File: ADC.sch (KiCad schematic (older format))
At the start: 15 parts

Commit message: Added multiple inputs
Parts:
- added C?: 47n, symbol C
- added C?: 4.7n, symbol C
- added C?: 4,7n, symbol C
- added C? (x7): 1n, symbol C
- added C?: 1u, symbol C
- added D? (x7): TVS, symbol TVS
- added P? (x3): CONN_01X03, symbol CONN_01X03
- added R? (x2): 4,7k, symbol R
- R?: value 1,65k -> 820
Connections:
- net +3V3: no longer U?.22 (AVDD)
- net GND: now also U?.10 (VREFCOM), U?.3 (CLK), C?.2
- net GNDA: now also C?.1, C?.1, C?.1, C?.1, C?.2, C?.2, C?.2, C?.2, D?.1, D?.1, D?.1, D?.1, D?.2, D?.2, D?.2
- net Iexc1: now reaches C?.1, C?.2, U?.11 (AIN0)
- net Iexc1: now also P?.2 (P2), U?.20 (IEXC1), C?.2, D?.2; no longer R?.1
- net at U?.13 (AIN4): now also C?.2, D?.2, P?.2 (P2)
- net at U?.14 (AIN5): now also C?.1, D?.1, P?.1 (P1)
- net at U?.15 (AIN6): now also C?.2, D?.2, P?.2 (P2)
- net at U?.16 (AIN7): now also C?.1, D?.1, P?.1 (P1)
- net at U?.17 (AIN2): now also C?.1, C?.2, R?.1
- net at U?.18 (AIN3): now also C?.1, C?.2, R?.1
- net Iexc2: now reaches U?.19 (IEXC2)
- net Iexc2: now also C?.1, D?.1, P?.1 (P1), R?.2
- net at U?.9 (VREFOUT): now also C?.1
- net at R?.2: no longer P?.2 (P2)
- net Vref: now reaches P?.3 (P3), R?.2, R?.2
- net Vref: now also P?.3 (P3), P?.3 (P3), P?.3 (P3)
- new net: C?.2, D?.2, P?.2 (P2), R?.2
- new net: C?.1, D?.1, P?.1 (P1), R?.2
- new net VDDA: U?.22 (AVDD)
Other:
- moved on the sheet: C?, D?, P?, R?

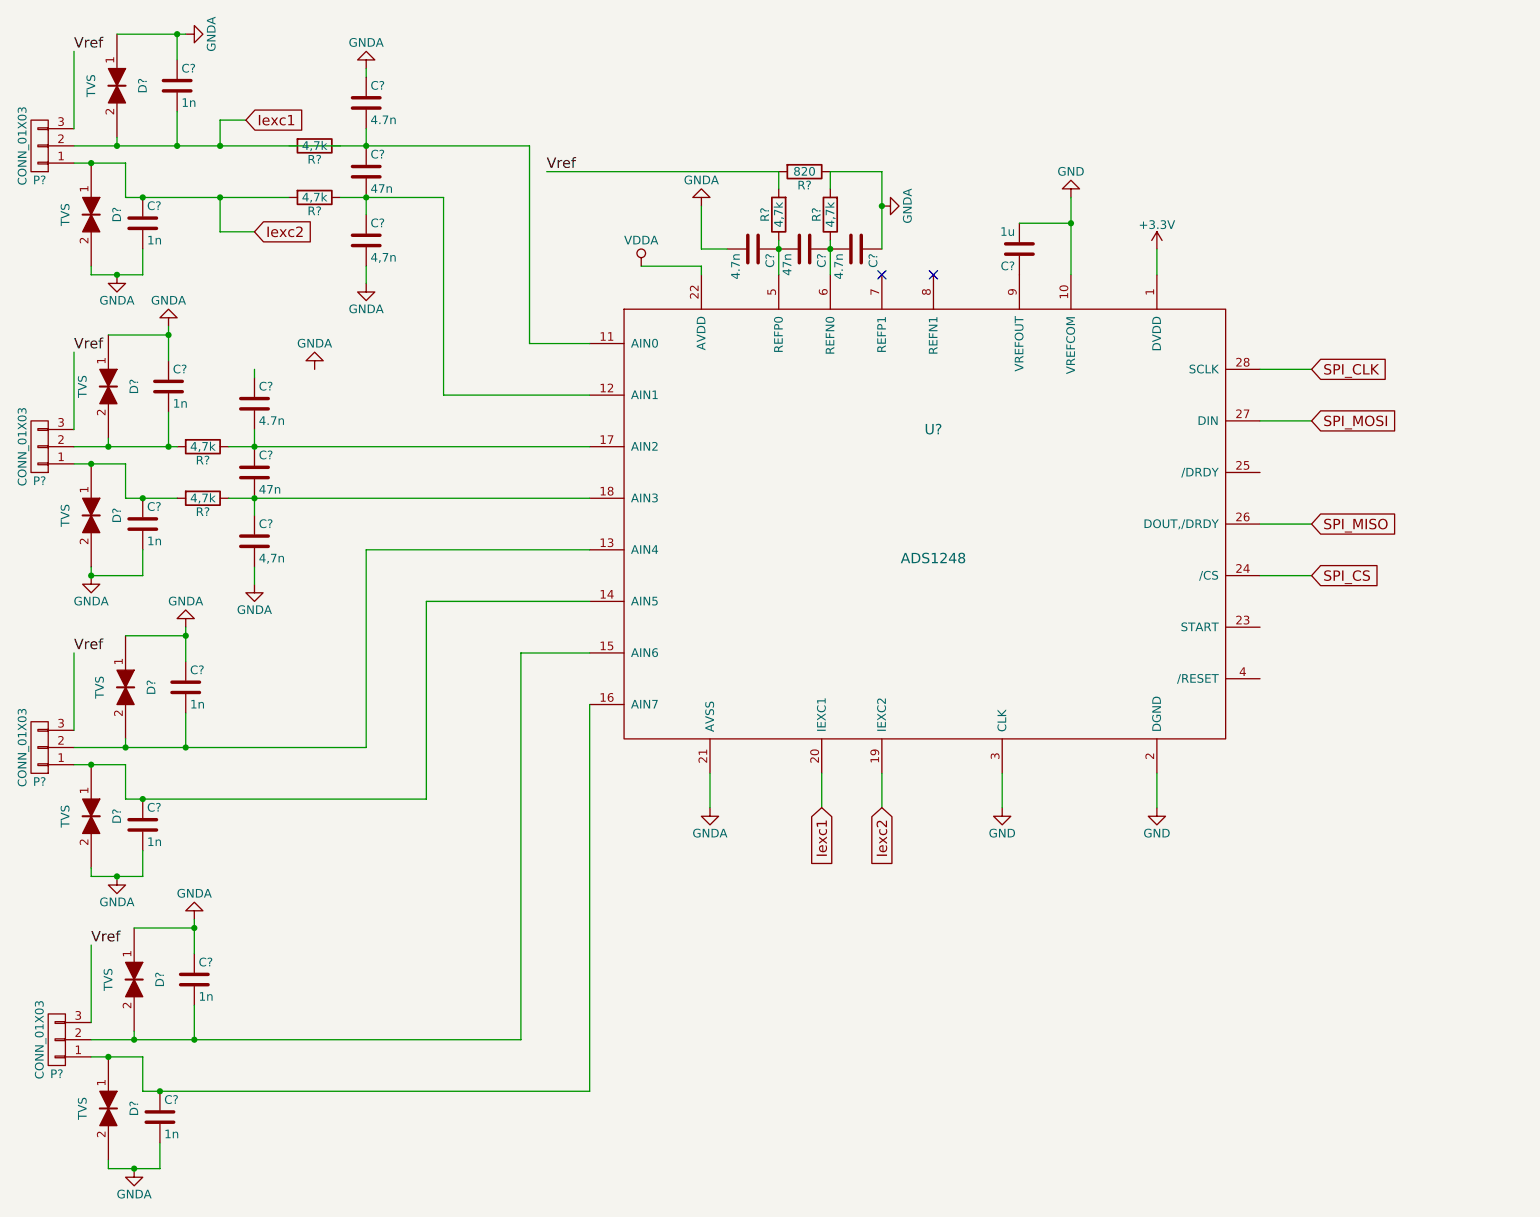
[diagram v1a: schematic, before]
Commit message: Peripherals added
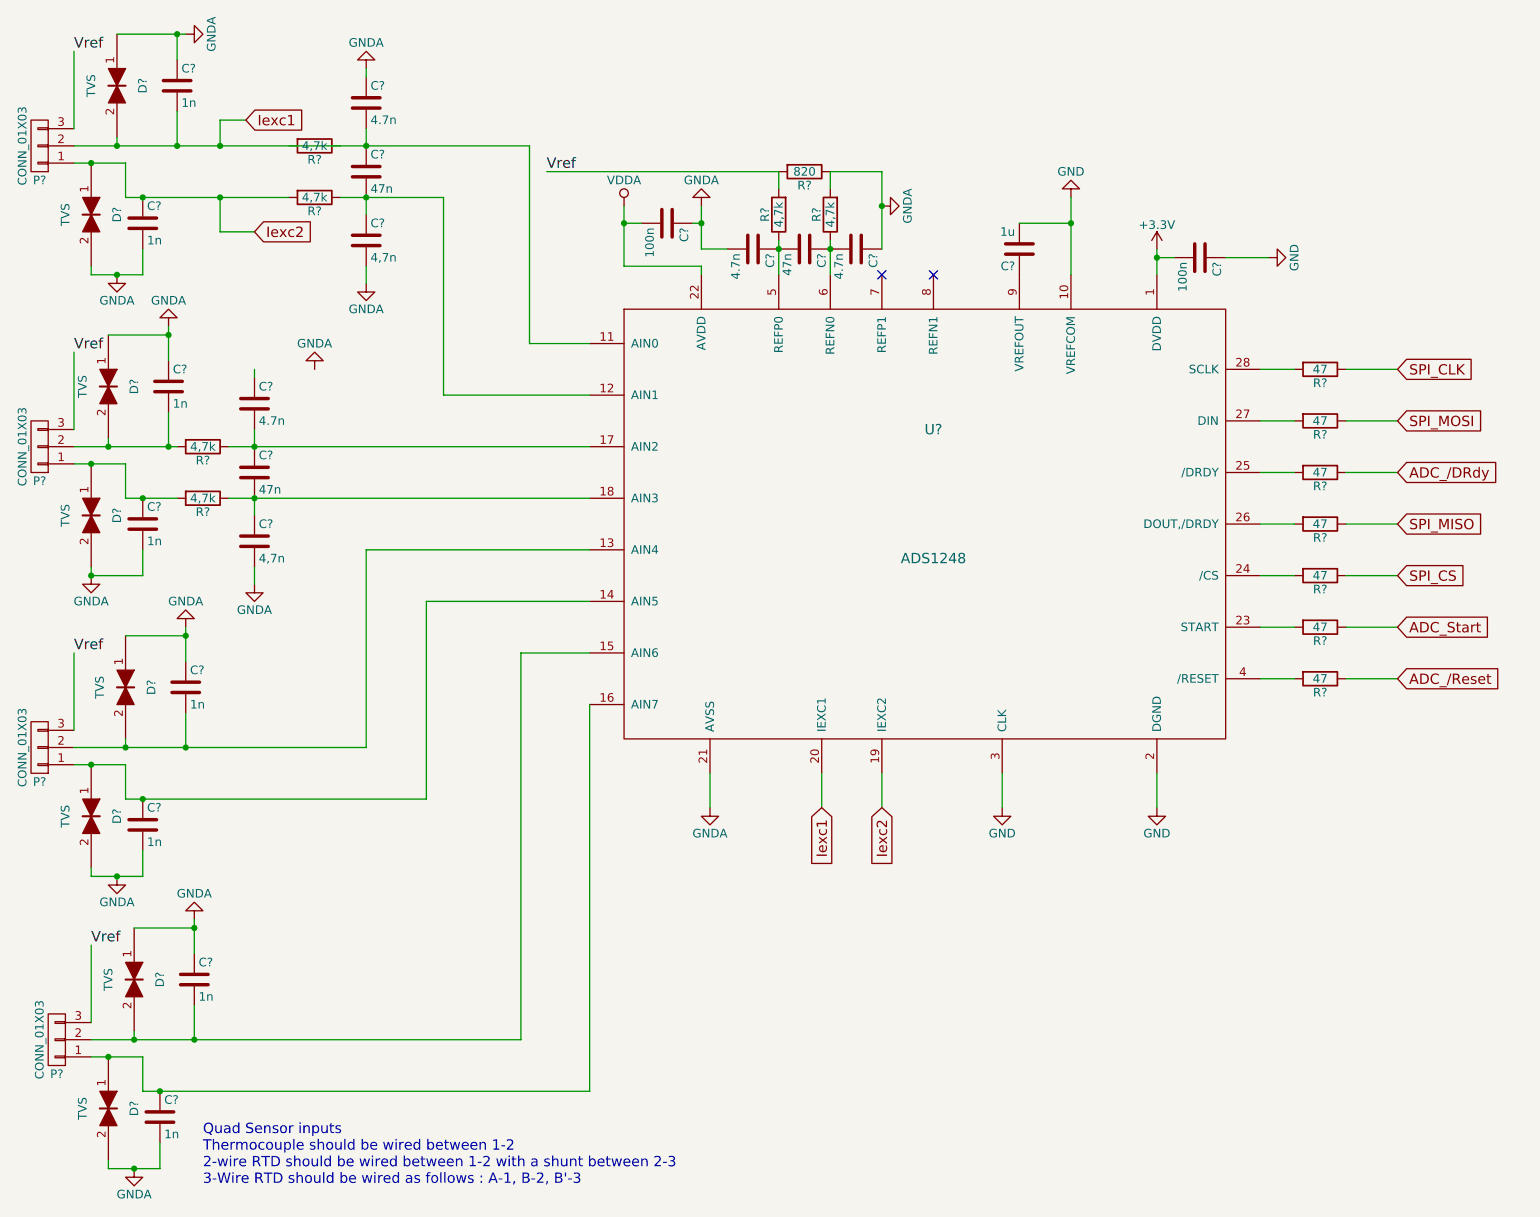
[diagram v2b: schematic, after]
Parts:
- added C? (x2): 100n, symbol C
- added R? (x7): 47, symbol R
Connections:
- net +3V3: now also C?.2
- net GND: now also C?.1
- net GNDA: now also C?.1
- net SPI_CLK: now also R?.1; no longer U?.28 (SCLK)
- net SPI_CS: now also R?.1; no longer U?.24 (/CS)
- net SPI_MISO: now also R?.1; no longer U?.26 (DOUT,/DRDY)
- net SPI_MOSI: now also R?.1; no longer U?.27 (DIN)
- net VDDA: now also C?.2
- net at U?.23 (START): now also R?.2
- net at U?.25 (/DRDY): now also R?.2
- net at U?.4 (/RESET): now also R?.2
- new net: R?.2, U?.24 (/CS)
- new net: R?.2, U?.26 (DOUT,/DRDY)
- new net: R?.2, U?.27 (DIN)
- new net: R?.2, U?.28 (SCLK)
- new net ADC_/DRdy: R?.1
- new net ADC_/Reset: R?.1
- new net ADC_Start: R?.1
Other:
- note added: "Quad Sensor inputs\nThermocouple should be wired between 1-2\n2-wire RTD should be wired between 1-2 with a shunt between 2-3\n3-Wire RTD should be wired as follows : A-1, B-2, B'-3"

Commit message: ADC values
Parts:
- C23, C26: renamed from C?; value 4.7n -> 47n
- C24, C27: renamed from C?; value 47n -> 470n
- C25, C28: renamed from C?; value 4,7n -> 47n
- C30, C32: renamed from C?; value 4.7n -> 3.3n
- C31: renamed from C?; value 47n -> 33n
- R33, R34, R35, R36: renamed from R?; value 4,7k -> 470
- R37, R39: renamed from R?; value 4,7k -> 10k
- gave numbers to parts that had none: 32
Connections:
- net GNDA: now also C23.1
- net Iexc1: now also R35.2; no longer C26.2, C27.1, U5.11 (AIN0)
- net at R35.1: now also C26.2, C27.1, U5.11 (AIN0)

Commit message: BOM
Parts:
- C15, C16, C17, C18, C19, C20, C21, C22, C23, C24, C25, C26, C27, C28, C29, C30, C31, C32, C33, C34: footprint (none) -> Capacitors_SMD:C_0805_HandSoldering
- D11, D12, D13, D14, D15, D16, D17, D18: value TVS -> ESD5Z3.3T1G; footprint (none) -> Diodes_SMD:D_SOD-523; symbol TVS -> D_Zener_ALT
- P10, P11, P8, P9: footprint (none) -> Connect:Fan_Pin_Header_Straight_1x03
- R33, R34, R35, R36, R37, R38: footprint (none) -> Resistors_SMD:R_0805_HandSoldering
- R39, R40, R41, R42, R43, R44, R45, R46: footprint (none) -> Resistors_SMD:R_0603_HandSoldering
- U5: footprint (none) -> Housings_SSOP:TSSOP-28_4.4x9.7mm_Pitch0.65mm
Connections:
- net GNDA: now also D14.2 (A), D16.2 (A), D17.2 (A), D18.2 (A); no longer D14.1, D16.1, D17.1, D18.1
- net Iexc1: now also D16.1 (K); no longer D16.2
- net at C21.2, P10.2 (P2), U5.13 (AIN4): now also D17.1 (K); no longer D17.2
- net at C22.2, P11.2 (P2), U5.15 (AIN6): now also D18.1 (K); no longer D18.2
- net at C19.2, P9.2 (P2), R33.2: now also D14.1 (K); no longer D14.2

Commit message: Continued simplifiying
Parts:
- removed C15, C16, C19, C20: 1n, Capacitors_SMD:C_0805_HandSoldering, symbol C
- removed C23, C25, C26, C28: 47n, Capacitors_SMD:C_0805_HandSoldering, symbol C
- removed C24, C27: 470n, Capacitors_SMD:C_0805_HandSoldering, symbol C
- removed D11, D12, D14, D16: ESD5Z3.3T1G, Diodes_SMD:D_SOD-523, symbol D_Zener_ALT
- removed P8, P9: CONN_01X03, Connect:Fan_Pin_Header_Straight_1x03, symbol CONN_01X03
- removed R33, R34, R35, R36: 470, Resistors_SMD:R_0805_HandSoldering, symbol R
- added P303, P304: CONN_01X03, Connectors:Fan_Pin_Header_Straight_1x03, symbol CONN_01X03
- P301: renamed from P10; footprint Connect:Fan_Pin_Header_Straight_1x03 -> Connectors:Fan_Pin_Header_Straight_1x03
- P302: renamed from P11; footprint Connect:Fan_Pin_Header_Straight_1x03 -> Connectors:Fan_Pin_Header_Straight_1x03
- renumbered C17 to C301, C18 to C302, C21 to C303, C22 to C304, C29 to C305, C30 to C306, C31 to C307, C32 to C308, C33 to C309, C34 to C310, D13 to D301, D15 to D302, D17 to D303, D18 to D304, R37 to R301, R38 to R302, R39 to R303, R40 to R304, R41 to R305, R42 to R306, R43 to R307, R44 to R308, R45 to R309, R46 to R310, U5 to U301
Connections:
- net Vref: now also P303.3 (P3), P304.3 (P3); no longer R301.2, R302.2
- net at U301.11 (AIN0): now also P303.2 (P2)
- net at U301.12 (AIN1): now also P303.1 (P1)
- net at U301.17 (AIN2): now also P304.2 (P2)
- net at U301.18 (AIN3): now also P304.1 (P1)
- new net: R301.2, R302.2
